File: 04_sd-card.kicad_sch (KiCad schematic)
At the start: 6 parts, among them J1 Micro_SD_Card_Det2

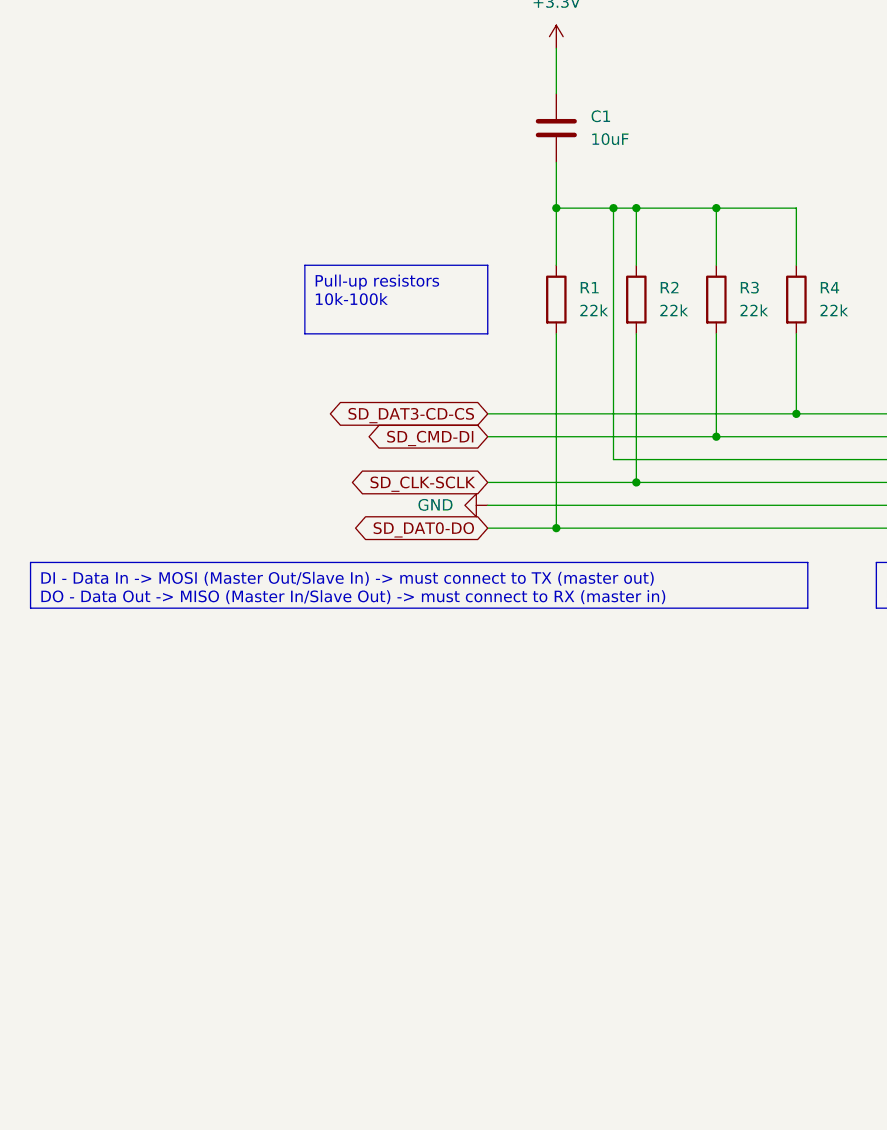
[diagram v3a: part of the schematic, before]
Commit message: Added some more notes, testpoints and rechecked footprints and parts
Signed-off-by: Anna-Lena Marx <anna-lena.marx@web.de>
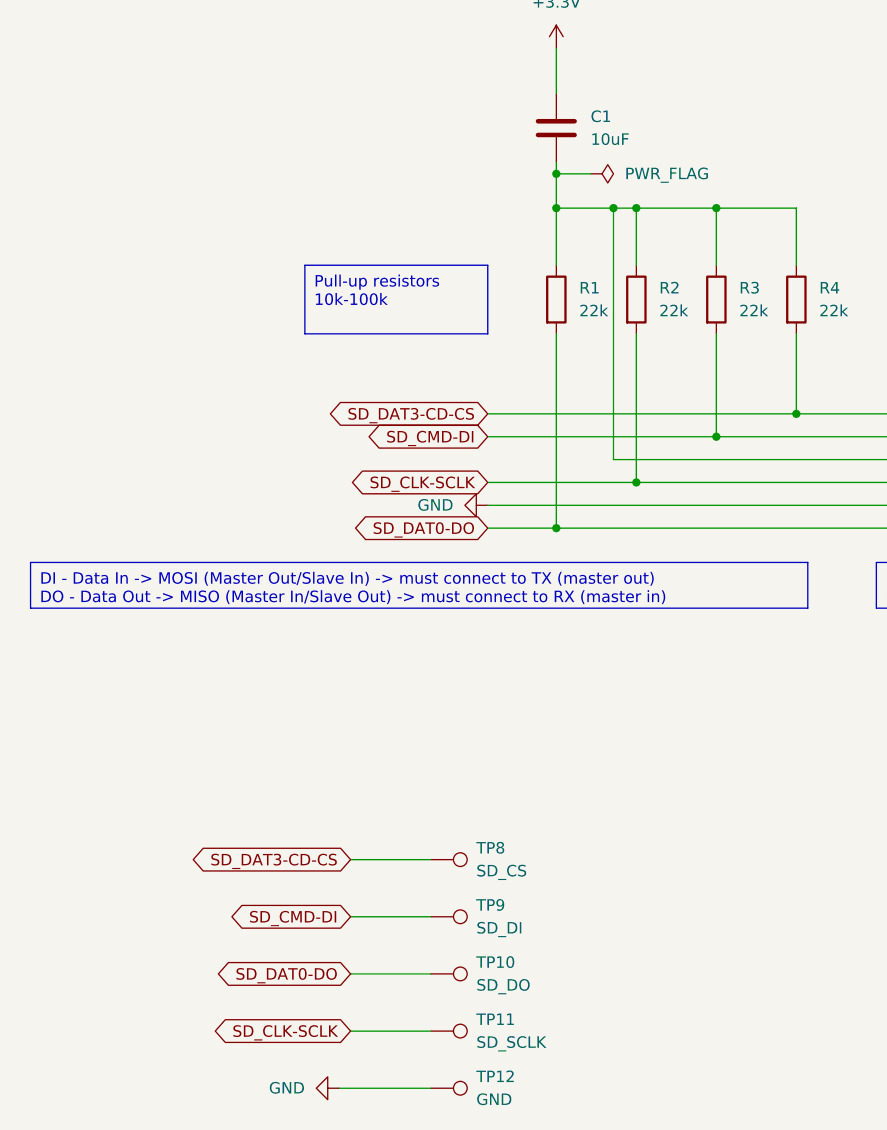
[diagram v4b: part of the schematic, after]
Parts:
- added TP10: SD_DO, TestPoint:TestPoint_Plated_Hole_D2.0mm, symbol Connector:TestPoint
- added TP11: SD_SCLK, TestPoint:TestPoint_Plated_Hole_D2.0mm, symbol Connector:TestPoint
- added TP12: GND, TestPoint:TestPoint_Plated_Hole_D2.0mm, symbol Connector:TestPoint
- added TP8: SD_CS, TestPoint:TestPoint_Plated_Hole_D2.0mm, symbol Connector:TestPoint
- added TP9: SD_DI, TestPoint:TestPoint_Plated_Hole_D2.0mm, symbol Connector:TestPoint
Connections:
- net GND: now also TP12.1
- net SD_CLK-SCLK: now also TP11.1
- net SD_CMD-DI: now also TP9.1
- net SD_DAT0-DO: now also TP10.1
- net SD_DAT3-CD-CS: now also TP8.1

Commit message: Changed buttons to smaller ones, updated some comments
Signed-off-by: Anna-Lena Marx <anna-lena.marx@web.de>
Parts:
- renumbered TP10 to TP10_SD_DO1, TP11 to TP11_SD_CLK1, TP12 to TP12_GND1, TP8 to TP8_SD_CS1, TP9 to TP9_SD_DI1
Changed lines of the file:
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@@
 		(dnp no)
 		(fields_autoplaced yes)
-		(property "Reference" "TP10"
+		(property "Reference" "TP10_SD_DO1"
 			(at 87.63 151.1299 90)
 			(effects
@@
 			(project "ZEReader-Pico"
 				(path "/ec954637-2a8b-4662-b4a1-f88107f11cb0/5fd074b7-3c47-4717-bcdc-b0d8134ff74e"
-					(reference "TP10")
+					(reference "TP10_SD_DO1")
 					(unit 1)
 				)
@@
 		(dnp no)
 		(fields_autoplaced yes)
-		(property "Reference" "TP9"
+		(property "Reference" "TP9_SD_DI1"
 			(at 87.63 144.7799 90)
 			(effects
@@
 			(project "ZEReader-Pico"
 				(path "/ec954637-2a8b-4662-b4a1-f88107f11cb0/5fd074b7-3c47-4717-bcdc-b0d8134ff74e"
-					(reference "TP9")
+					(reference "TP9_SD_DI1")
 					(unit 1)
 				)
@@
 		(dnp no)
 		(fields_autoplaced yes)
-		(property "Reference" "TP8"
+		(property "Reference" "TP8_SD_CS1"
 			(at 87.63 138.4299 90)
 			(effects
@@
 			(project "ZEReader-Pico"
 				(path "/ec954637-2a8b-4662-b4a1-f88107f11cb0/5fd074b7-3c47-4717-bcdc-b0d8134ff74e"
-					(reference "TP8")
+					(reference "TP8_SD_CS1")
 					(unit 1)
 				)
@@
 		(dnp no)
 		(fields_autoplaced yes)
-		(property "Reference" "TP11"
+		(property "Reference" "TP11_SD_CLK1"
 			(at 87.63 157.4799 90)
 			(effects
@@
 			(project "ZEReader-Pico"
 				(path "/ec954637-2a8b-4662-b4a1-f88107f11cb0/5fd074b7-3c47-4717-bcdc-b0d8134ff74e"
-					(reference "TP11")
+					(reference "TP11_SD_CLK1")
 					(unit 1)
 				)
@@
 		(dnp no)
 		(fields_autoplaced yes)
-		(property "Reference" "TP12"
+		(property "Reference" "TP12_GND1"
 			(at 87.63 163.8299 90)
 			(effects
@@
 			(project "ZEReader-Pico"
 				(path "/ec954637-2a8b-4662-b4a1-f88107f11cb0/5fd074b7-3c47-4717-bcdc-b0d8134ff74e"
-					(reference "TP12")
-					(unit 1)
-				)
+					(reference "TP12_GND1")
+					(unit 1)
+				)

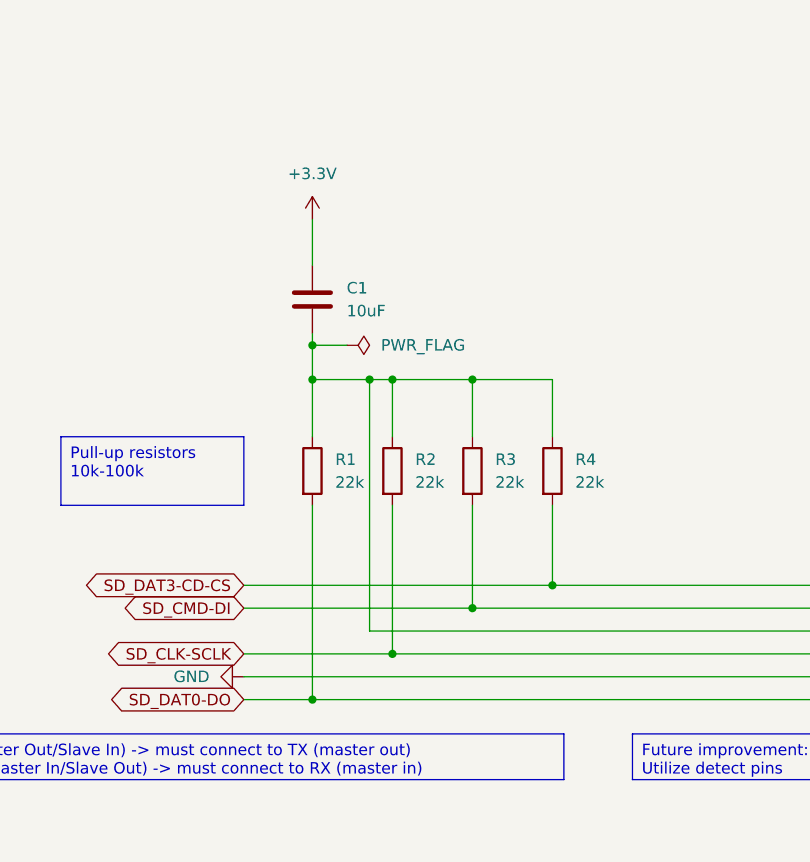
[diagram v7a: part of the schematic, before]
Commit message: Redesigned SD Reader and Buttons
Signed-off-by: Anna-Lena Marx <anna-lena.marx@web.de>
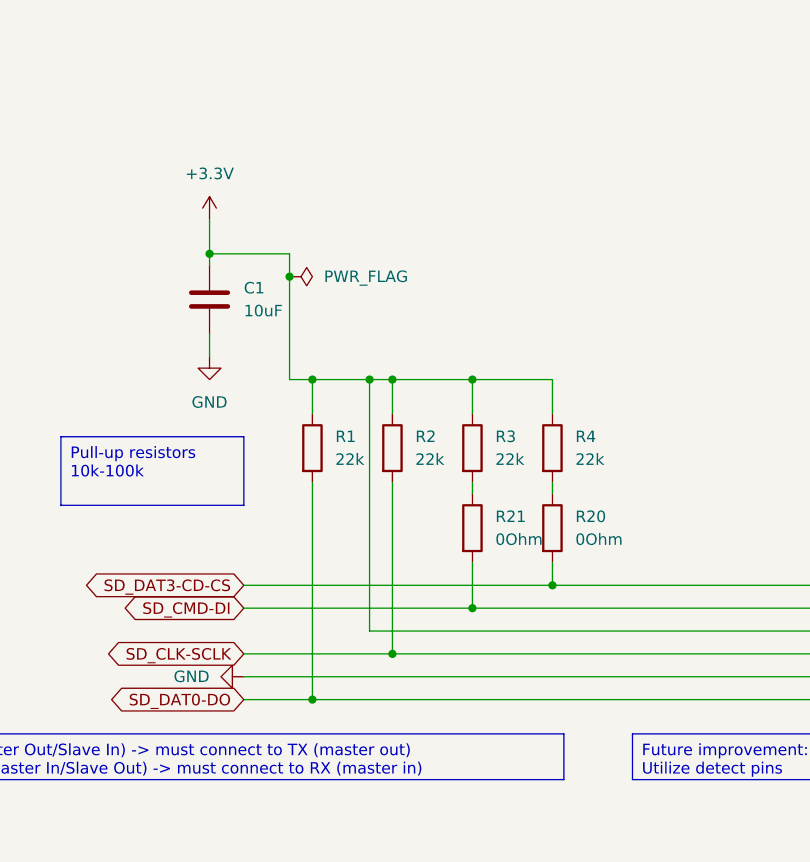
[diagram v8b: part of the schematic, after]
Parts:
- added R20, R21: 0Ohm, Resistor_SMD:R_1206_3216Metric_Pad1.30x1.75mm_HandSolder, symbol Device:R
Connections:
- net +3.3V: now also J1.4 (VDD), R1.1, R2.1, R3.1, R4.1
- net GND: now also C1.2
- net SD_CMD-DI: now also R21.2; no longer R3.2
- net SD_DAT3-CD-CS: now also R20.2; no longer R4.2
- new net: R20.1, R4.2
- new net: R21.1, R3.2
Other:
- moved on the sheet: C1, R1, R2, R3, R4
